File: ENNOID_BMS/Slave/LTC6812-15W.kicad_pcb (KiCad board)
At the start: 2 copper layers, 73.4 x 117.4 mm, 255 parts, among them J1 PB MB 2, J10 PB MB 1, J11 PA MA 1, J2 PA MA 2, J3 Sensors, J4 Conn_01x08, J5 Conn_01x08, J6 Sensors, Q1 DZTT5551, Q10 TSM2323, Q11 TSM2323, Q12 TSM2323, Q13 TSM2323, Q14 TSM2323, Q15 TSM2323, Q16 TSM2323, Q17 DZTT5551, Q18 2N7002, Q19 2N7002, Q2 TSM2323, Q20 2N7002, Q21 2N7002, Q22 2N7002, Q23 2N7002, Q24 2N7002, Q25 2N7002, Q26 2N7002, Q27 2N7002, Q28 2N7002, Q29 2N7002, Q3 TSM2323, Q30 2N7002, Q31 2N7002, Q32 2N7002, Q4 TSM2323, Q5 TSM2323, Q6 TSM2323, Q7 TSM2323, Q8 TSM2323, Q9 TSM2323, U1 LTC6812-1, U2 LTC6812-1

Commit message: master and slave updated
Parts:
- removed F19, F53, F65: 50mA, Fuse:Fuse_0603_1608Metric
- F1, F11, F13, F15, F18, F20, F22, F24, F26, F28, F3, F30, F32, F34, F35, F37, F39, F41, F44, F46, F47, F49, F5, F51, F55, F57, F59, F61, F63, F64, F66, F67, F7, F9: footprint Fuse:Fuse_0603_1608Metric -> Fuse:Fuse_1206_3216Metric
- moved F18 63.8 mm to (73.4, 42.2), turned to 0 degrees
- moved F1 44.8 mm to (73.4, 44.7), turned to 0 degrees
- moved F66 22.3 mm to (67.8, 64.0)
- moved D17 5.00 mm to (71.6, 65.8)
- moved D8 4.99 mm to (72.2, 116.8)
- moved D16 4.93 mm to (71.6, 71.5)
- moved D7 4.92 mm to (72.2, 122.5)
- moved D18 4.89 mm to (71.7, 60.0)
- moved D5 4.85 mm to (72.4, 133.1)
- moved D19 4.82 mm to (71.5, 53.9)
- moved D6 4.76 mm to (72.3, 127.8)
- moved D15 4.73 mm to (71.6, 76.8)
- moved D14 4.71 mm to (71.7, 83.4)
- moved D9 4.67 mm to (71.9, 111.5)
- moved D12 4.67 mm to (71.8, 94.5)
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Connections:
- C1 pad 2: Net-(C1-Pad2) -> Net-(U1-V+)
- C10 pad 2: Net-(C10-Pad2) -> Net-(U2-V+)
- C11 pad 2: Net-(D5-K) -> /cell1/C
- C12 pad 2: Net-(D6-K) -> /cell2/C
- C13 pad 2: Net-(D7-K) -> /cell3/C
- C14 pad 2: Net-(D8-K) -> /cell4/C
- C15 pad 2: Net-(D9-K) -> /cell5/C
- C16 pad 2: Net-(D10-K) -> /cell6/C
- C17 pad 2: Net-(D11-K) -> /cell7/C
- C18 pad 2: Net-(D12-K) -> /cell8/C
- C19 pad 2: Net-(D13-K) -> /cell10/CM
- C20 pad 2: Net-(D14-K) -> /cell10/C
- C21 pad 2: Net-(D15-K) -> /cell11/C
- C22 pad 2: Net-(D16-K) -> /cell12/C
- C23 pad 2: Net-(D17-K) -> /cell13/C
- C24 pad 2: Net-(D18-K) -> /cell14/C
- C25 pad 2: Net-(D19-K) -> /cell15/C
- C29 pad 2: Net-(Q17-E) -> /Vreg_2
- C30 pad 2: Net-(Q17-E) -> /Vreg_2
- C31 pad 2: Net-(Q17-E) -> /Vreg_2
- C5 pad 2: Net-(Q1-E) -> /Vreg_1
- C6 pad 2: Net-(Q1-E) -> /Vreg_1
- C7 pad 2: Net-(Q1-E) -> /Vreg_1
- D10 pad 1: Net-(D10-K) -> /cell6/C
- D11 pad 1: Net-(D11-K) -> /cell7/C
- D12 pad 1: Net-(D12-K) -> /cell8/C
- D13 pad 1: Net-(D13-K) -> /cell10/CM
- D14 pad 1: Net-(D14-K) -> /cell10/C
- D15 pad 1: Net-(D15-K) -> /cell11/C
- D16 pad 1: Net-(D16-K) -> /cell12/C
- D17 pad 1: Net-(D17-K) -> /cell13/C
- D18 pad 1: Net-(D18-K) -> /cell14/C
- D19 pad 1: Net-(D19-K) -> /cell15/C
- D5 pad 1: Net-(D5-K) -> /cell1/C
- D6 pad 1: Net-(D6-K) -> /cell2/C
- D7 pad 1: Net-(D7-K) -> /cell3/C
- D8 pad 1: Net-(D8-K) -> /cell4/C
- D9 pad 1: Net-(D9-K) -> /cell5/C
- F1 pad 1: Net-(C1-Pad2) -> Net-(F1-Pad1)
- F11 pad 1: Net-(D15-K) -> Net-(F11-Pad1)
- F13 pad 1: Net-(D14-K) -> Net-(F13-Pad1)
- F15 pad 1: Net-(D13-K) -> Net-(F15-Pad1)
- F18 pad 1: Net-(Q1-E) -> Net-(F18-Pad1)
- F18 pad 2: /Vreg_1 -> Net-(C4-Pad2)
- F20 pad 1: Net-(D12-K) -> Net-(F20-Pad1)
- F22 pad 1: Net-(D11-K) -> Net-(F22-Pad1)
- F24 pad 1: Net-(D10-K) -> Net-(F24-Pad1)
- F26 pad 1: Net-(D9-K) -> Net-(F26-Pad1)
- F28 pad 1: Net-(D8-K) -> Net-(F28-Pad1)
- F3 pad 1: Net-(D19-K) -> Net-(F3-Pad1)
- F30 pad 1: Net-(D7-K) -> Net-(F30-Pad1)
- F32 pad 1: Net-(D6-K) -> Net-(F32-Pad1)
- F34 pad 1: Net-(D5-K) -> Net-(F34-Pad1)
- F5 pad 1: Net-(D18-K) -> Net-(F5-Pad1)
- F66 pad 1: /Vreg_2 -> Net-(C28-Pad2)
- F66 pad 2: Net-(Q17-E) -> Net-(F66-Pad2)
- F67 pad 1: Net-(C10-Pad2) -> Net-(F67-Pad1)
- F7 pad 1: Net-(D17-K) -> Net-(F7-Pad1)
- F9 pad 1: Net-(D16-K) -> Net-(F9-Pad1)
- Q1 pad 3: Net-(Q1-E) -> /Vreg_1
- Q17 pad 3: Net-(Q17-E) -> /Vreg_2
- R1 pad 1: Net-(C1-Pad2) -> Net-(F1-Pad1)
- R15 pad 1: Net-(D5-K) -> Net-(F34-Pad1)
- R19 pad 1: Net-(D6-K) -> Net-(F32-Pad1)
- R23 pad 1: Net-(D7-K) -> Net-(F30-Pad1)
- R27 pad 1: Net-(D8-K) -> Net-(F28-Pad1)
- R3 pad 1: Net-(C4-Pad2) -> Net-(F18-Pad1)
- R31 pad 1: Net-(D9-K) -> Net-(F26-Pad1)
- R35 pad 1: Net-(D10-K) -> Net-(F24-Pad1)
- R39 pad 1: Net-(D11-K) -> Net-(F22-Pad1)
- R43 pad 1: Net-(D12-K) -> Net-(F20-Pad1)
- R47 pad 1: Net-(D13-K) -> Net-(F15-Pad1)
- R51 pad 1: Net-(D14-K) -> Net-(F13-Pad1)
- R55 pad 1: Net-(D15-K) -> Net-(F11-Pad1)
- R59 pad 1: Net-(D16-K) -> Net-(F9-Pad1)
- R63 pad 1: Net-(D17-K) -> Net-(F7-Pad1)
- R67 pad 1: Net-(D18-K) -> Net-(F5-Pad1)
- R71 pad 1: Net-(D19-K) -> Net-(F3-Pad1)
- R74 pad 1: Net-(C10-Pad2) -> Net-(F67-Pad1)
- R76 pad 1: Net-(C28-Pad2) -> Net-(F66-Pad2)
- U1 pad 65: Net-(U1-V-) -> Cell_1-
- U2 pad 38: Net-(U2-C0) -> Cell_1-
- U2 pad 65: Net-(U2-V-) -> Cell_1-
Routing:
- net Net-(C1-Pad2): track 51.2 -> 0.00 mm
- net Net-(U1-V+): track 2.18 -> 50.9 mm
- net Net-(Q17-E): track 48.6 -> 0.00 mm
- net /Vreg_2: track 28.7 -> 71.4 mm
- net Net-(Q1-E): track 16.0 -> 0.00 mm
- net /Vreg_1: track 27.9 -> 40.3 mm
- net Net-(U1-V-): track 10.1 -> 0.00 mm
- net Net-(U2-V-): track 10.0 -> 0.00 mm
- net Cell_1-: track 78.0 -> 69.8 mm, vias 23 -> 9
- net Net-(D14-K): track 7.68 -> 0.00 mm
- net Net-(D13-K): track 7.23 -> 0.00 mm
- net Net-(D7-K): track 7.00 -> 0.00 mm
- net Net-(D12-K): track 6.77 -> 0.00 mm
- net Net-(D8-K): track 6.72 -> 0.00 mm
- net Net-(D5-K): track 6.62 -> 0.00 mm
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
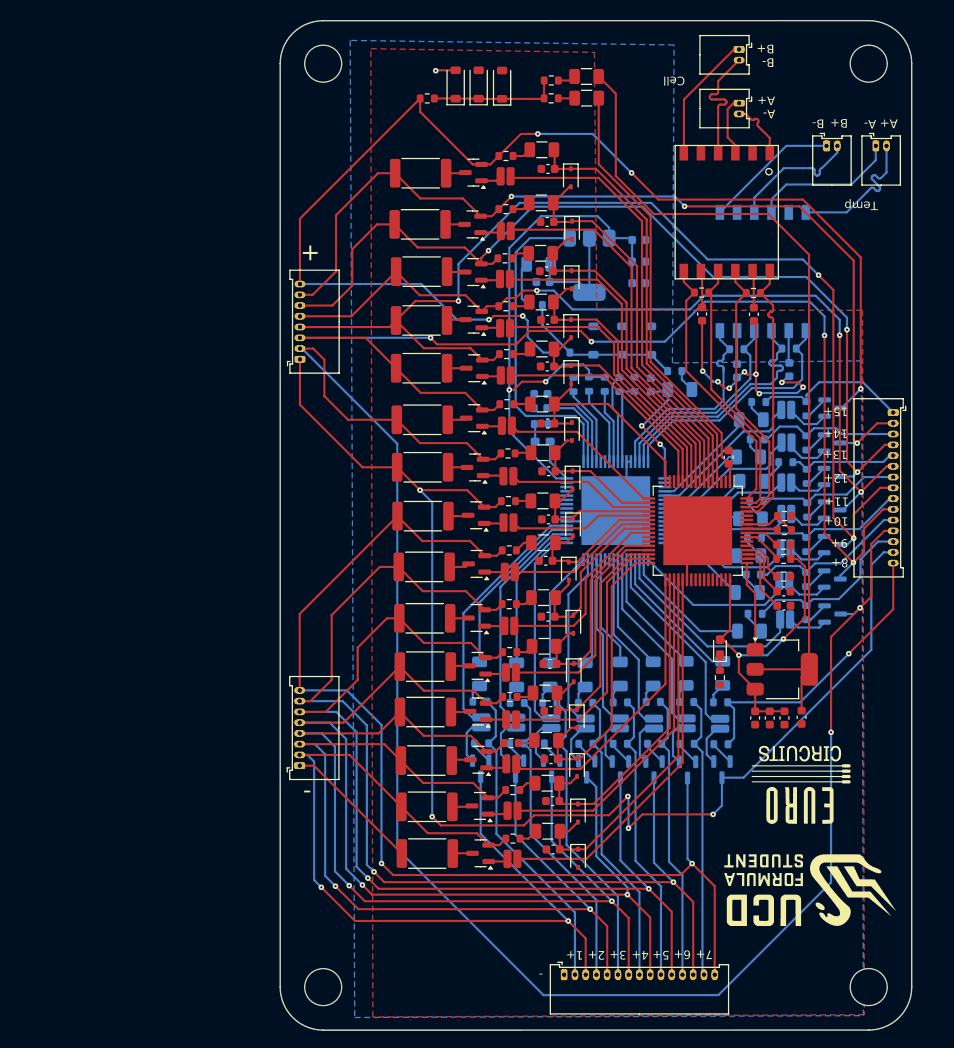
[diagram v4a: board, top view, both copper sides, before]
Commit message: new cells and updated slave
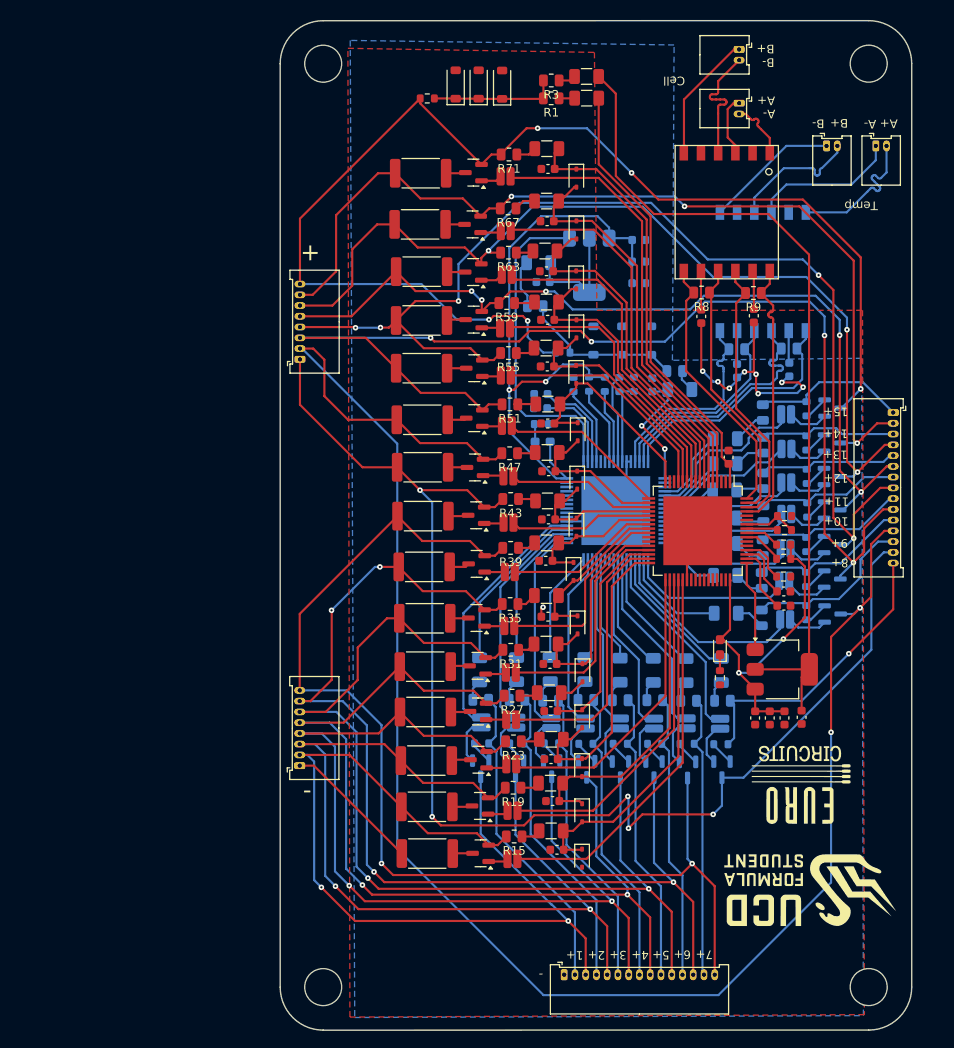
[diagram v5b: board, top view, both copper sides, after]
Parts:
- R1, R15, R19, R23, R27, R3, R31, R35, R39, R43, R47, R51, R55, R59, R63, R67, R71, R74, R76, R8, R81, R82, R84, R85, R86, R87, R88, R89, R9, R90, R91, R92, R93, R94, R95, R96, R98, R99: footprint Resistor_SMD:R_0603_1608Metric -> Resistor_SMD:R_0805_2012Metric
- moved F63 3.74 mm to (89.5, 84.3)
- moved F35 3.42 mm to (89.6, 104.6)
- moved R86 3.40 mm to (93.9, 89.2), turned to 90 degrees
- moved F59 3.35 mm to (89.4, 90.2)
- moved F64 3.23 mm to (89.5, 100.2)
- moved F55 3.09 mm to (89.5, 96.5)
- moved F57 3.00 mm to (89.4, 93.5)
- moved F61 2.84 mm to (89.5, 87.2)
- moved R87 1.68 mm to (93.9, 93.0), turned to 90 degrees
- moved R88 1.47 mm to (93.8, 96.9), turned to 90 degrees
- moved R84 1.32 mm to (93.8, 81.2), turned to 90 degrees
- moved R89 1.19 mm to (93.7, 100.7), turned to 90 degrees
- moved D9 1.01 mm to (72.9, 111.5)
- moved R85 0.97 mm to (93.9, 85.0), turned to 90 degrees
- moved R90 0.90 mm to (93.7, 105.1), turned to 90 degrees
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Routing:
- net Net-(U2-C13): track 10.1 -> 6.45 mm
- net Meas13+: track 12.7 -> 16.1 mm
- net Net-(U2-C10): track 10.6 -> 7.23 mm
- net Net-(U2-C11): track 9.81 -> 6.48 mm
- net /cell6/C: track 22.5 -> 19.2 mm
- net Net-(U2-C9): track 15.4 -> 12.2 mm
- net Net-(U2-C15): track 12.5 -> 9.32 mm
- net Net-(U2-C12): track 8.64 -> 5.60 mm
- net Net-(U2-C14): track 10.4 -> 7.58 mm
- net /cell1/C: track 43.5 -> 41.9 mm
- net Cell_1-: track 69.8 -> 68.3 mm
- net /cell7/C: track 17.9 -> 16.5 mm
- net Net-(F63-Pad1): track 2.62 -> 3.85 mm
- net S15: track 18.3 -> 19.4 mm
- net S14: track 17.3 -> 16.2 mm
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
